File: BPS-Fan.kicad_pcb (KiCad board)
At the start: 2 copper layers, 45 x 34.5 mm, 21 parts, among them J1 LDRBRDConn, J2 FAN1, J3 FAN2, J4 FAN3, J5 FAN4, Q1 BUK9M34-100EX, Q2 BUK9M34-100EX, Q3 BUK9M34-100EX, Q4 BUK9M34-100EX

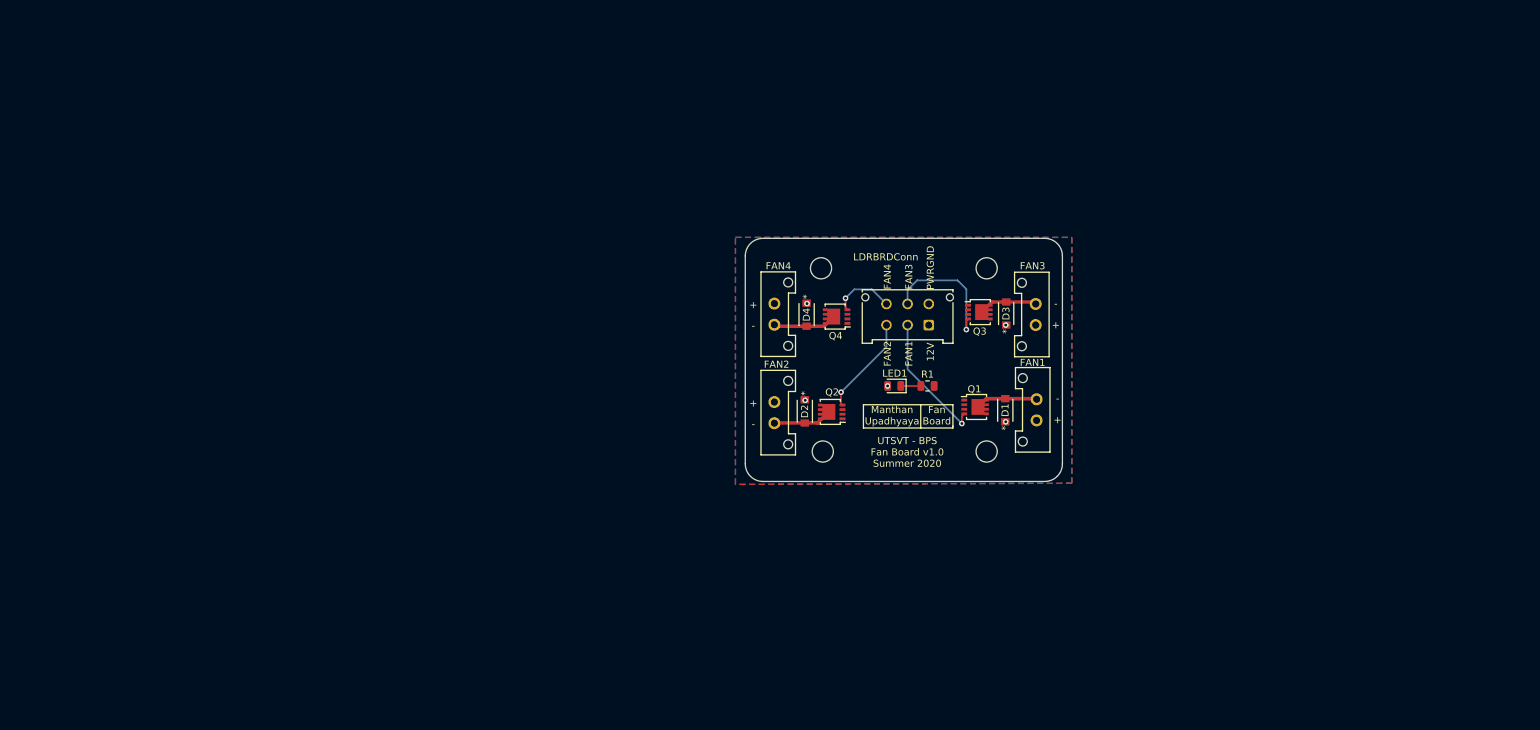
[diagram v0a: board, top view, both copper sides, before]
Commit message: Modified BPS fan pcb schematic to support 12 fans instead of 4.
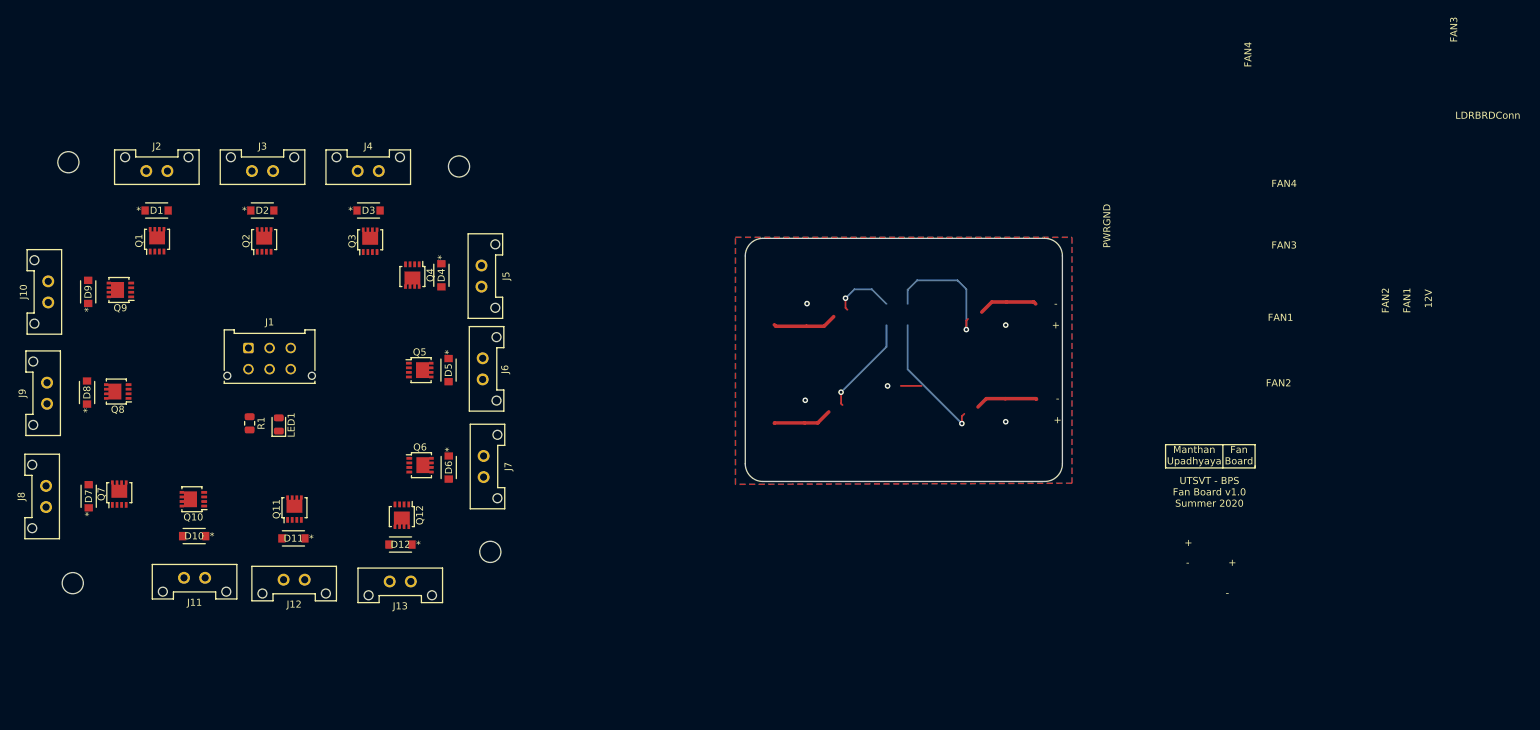
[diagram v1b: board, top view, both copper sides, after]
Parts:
- added D10: V2F22HM, UTSVT_Passive:V2F22HM, F.Cu at (56.8, 97.2)
- added D11: V2F22HM, UTSVT_Passive:V2F22HM, F.Cu at (70.9, 97.6)
- added D12: V2F22HM, UTSVT_Passive:V2F22HM, F.Cu at (86.1, 98.5)
- added D5: V2F22HM, UTSVT_Passive:V2F22HM, F.Cu at (92.9, 73.7)
- added D6: V2F22HM, UTSVT_Passive:V2F22HM, F.Cu at (92.9, 87.5)
- added D7: V2F22HM, UTSVT_Passive:V2F22HM, F.Cu at (41.8, 91.6)
- added D8: V2F22HM, UTSVT_Passive:V2F22HM, F.Cu at (41.6, 76.9)
- added D9: V2F22HM, UTSVT_Passive:V2F22HM, F.Cu at (41.8, 62.6)
- added J10: FAN9, UTSVT_Connectors:Molex_MicroFit3.0_1x2xP3.00mm_PolarizingPeg_Vertical, F.Cu at (36.1, 64.1)
- added J11: FAN10, UTSVT_Connectors:Molex_MicroFit3.0_1x2xP3.00mm_PolarizingPeg_Vertical, F.Cu at (58.4, 103.2)
- added J12: FAN11, UTSVT_Connectors:Molex_MicroFit3.0_1x2xP3.00mm_PolarizingPeg_Vertical, F.Cu at (72.5, 103.4)
- added J13: FAN12, UTSVT_Connectors:Molex_MicroFit3.0_1x2xP3.00mm_PolarizingPeg_Vertical, F.Cu at (87.5, 103.7)
- added J6: FAN5, UTSVT_Connectors:Molex_MicroFit3.0_1x2xP3.00mm_PolarizingPeg_Vertical, F.Cu at (97.7, 72.0)
- added J7: FAN6, UTSVT_Connectors:Molex_MicroFit3.0_1x2xP3.00mm_PolarizingPeg_Vertical, F.Cu at (97.9, 85.9)
- added J8: FAN7, UTSVT_Connectors:Molex_MicroFit3.0_1x2xP3.00mm_PolarizingPeg_Vertical, F.Cu at (35.8, 93.1)
- added J9: FAN8, UTSVT_Connectors:Molex_MicroFit3.0_1x2xP3.00mm_PolarizingPeg_Vertical, F.Cu at (35.9, 78.5)
- added Q10: BUK9M34-100EX, Package_TO_SOT_SMD:LFPAK33, F.Cu at (56.7, 92.0)
- added Q11: BUK9M34-100EX, Package_TO_SOT_SMD:LFPAK33, F.Cu at (71.0, 93.4)
- added Q12: BUK9M34-100EX, Package_TO_SOT_SMD:LFPAK33, F.Cu at (86.3, 94.3)
- added Q5: BUK9M34-100EX, Package_TO_SOT_SMD:LFPAK33, F.Cu at (88.8, 73.7)
- added Q6: BUK9M34-100EX, Package_TO_SOT_SMD:LFPAK33, F.Cu at (88.8, 87.2)
- added Q7: BUK9M34-100EX, Package_TO_SOT_SMD:LFPAK33, F.Cu at (46.2, 91.3)
- added Q8: BUK9M34-100EX, Package_TO_SOT_SMD:LFPAK33, F.Cu at (46.0, 76.7)
- added Q9: BUK9M34-100EX, Package_TO_SOT_SMD:LFPAK33, F.Cu at (46.3, 62.3)
- moved J2 131.2 mm to (50.0, 45.5), turned to 0 degrees
- moved H4 131.0 mm to (39.6, 103.9)
- moved D1 123.7 mm to (51.5, 51.0), turned to 0 degrees
- moved Q1 118.5 mm to (51.5, 55.3), turned to 90 degrees
- moved H1 107.9 mm to (39.0, 44.2)
- moved J4 98.7 mm to (80.0, 45.5), turned to 0 degrees
- moved J1 96.6 mm to (64.5, 70.6), turned to 0 degrees
- moved R1 96.3 mm to (64.7, 81.2), turned to -90 degrees
- moved D3 91.7 mm to (81.5, 51.0), turned to 0 degrees
- moved LED1 87.5 mm to (68.8, 81.4), turned to 90 degrees
- moved Q3 87.0 mm to (81.8, 55.4), turned to 90 degrees
- moved Q2 84.1 mm to (66.7, 55.4), turned to 90 degrees
- moved D2 82.1 mm to (66.5, 51.0), turned to 0 degrees
- moved J3 81.1 mm to (65.0, 45.5), turned to 0 degrees
- moved H3 76.3 mm to (94.4, 44.8)
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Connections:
- D1 pad 1: +12V -> Net-(J2-Pad1)
- D2 pad 1: +12V -> Net-(J2-Pad1)
- D3 pad 1: +12V -> Net-(J2-Pad1)
- D4 pad 1: +12V -> GNDPWR
- J1 pad 2: /FAN1 -> /FAN1CONN
- J1 pad 3: /FAN2 -> /FAN2CONN
- J1 pad 5: /FAN3 -> /FAN3CONN
- J1 pad 6: /FAN4 -> /FAN4CONN
- J2 pad 1: +12V -> Net-(J2-Pad1)
- J3 pad 1: +12V -> Net-(J2-Pad1)
- J4 pad 1: +12V -> Net-(J2-Pad1)
- J5 pad 1: +12V -> GNDPWR
- Q1 pad 4: /FAN1 -> /FAN1CONN
- Q2 pad 4: /FAN2 -> /FAN1CONN
- Q3 pad 4: /FAN3 -> /FAN1CONN
- Q4 pad 4: /FAN4 -> /FAN2CONN
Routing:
- net (no net): track 0.00 -> 46.3 mm, vias 0 -> 2
- net /FAN3: track 18.7 -> 0.00 mm, vias 1 -> 0
- net /FAN1: track 18.7 -> 0.00 mm, vias 1 -> 0
- net Net-(J6-Pad2): track 0.00 -> 14.1 mm, vias 0 -> 1
- net /FAN2: track 14.1 -> 0.00 mm, vias 1 -> 0
- net Net-(J5-Pad2): track 9.08 -> 0.00 mm
- net Net-(J2-Pad1): track 0.00 -> 9.08 mm
- net Net-(D3-Pad2): track 8.37 -> 17.4 mm, vias 0 -> 1
- net /FAN4: track 9.05 -> 0.00 mm, vias 1 -> 0
- net Net-(J2-Pad2): track 8.84 -> 0.00 mm
- net Net-(J3-Pad2): track 8.39 -> 0.00 mm
- net GNDPWR: track 0.00 -> 8.39 mm
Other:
- net class Default removed

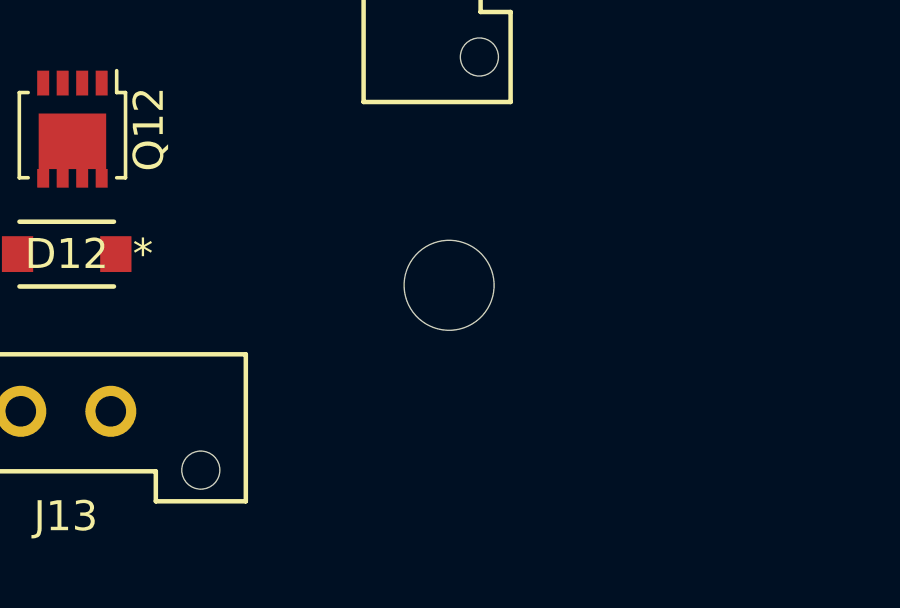
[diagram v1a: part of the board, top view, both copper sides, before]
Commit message: Replaced mosfet, added Hannah's changes, updated bom and data sheets
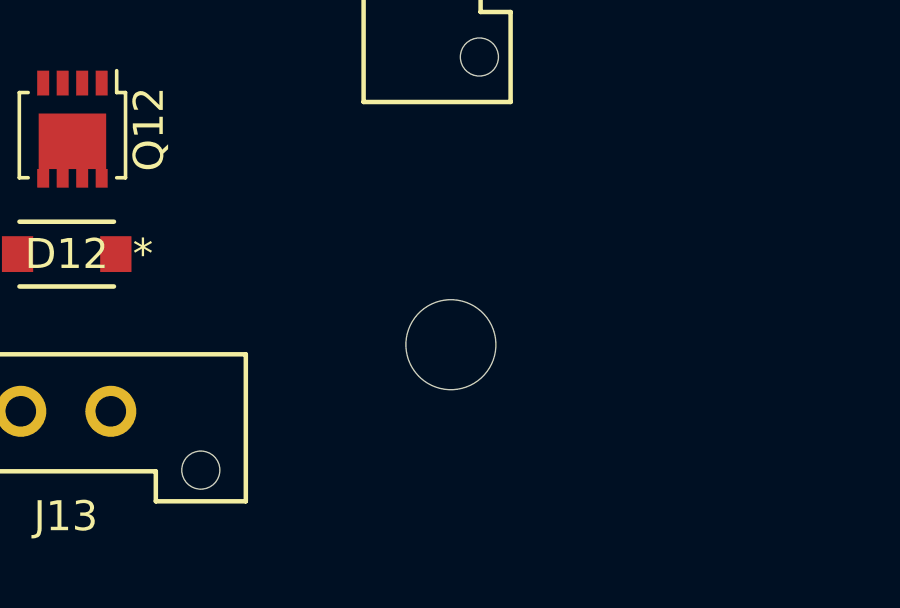
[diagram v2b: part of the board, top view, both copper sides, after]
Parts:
- Q1, Q10, Q11, Q12, Q2, Q3, Q4, Q5, Q6, Q7, Q8, Q9: value BUK9M34-100EX -> BUK9M23-80E
- moved H2 1.98 mm to (98.9, 101.5)
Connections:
- D1 pad 1: Net-(J2-Pad1) -> +12V
- D10 pad 1: GNDPWR -> +12V
- D11 pad 1: GNDPWR -> +12V
- D12 pad 1: GNDPWR -> +12V
- D2 pad 1: Net-(J2-Pad1) -> +12V
- D3 pad 1: Net-(J2-Pad1) -> +12V
- D4 pad 1: GNDPWR -> +12V
- D5 pad 1: GNDPWR -> +12V
- D6 pad 1: GNDPWR -> +12V
- D7 pad 1: GNDPWR -> +12V
- D8 pad 1: GNDPWR -> +12V
- D9 pad 1: GNDPWR -> +12V
- J10 pad 1: GNDPWR -> +12V
- J11 pad 1: GNDPWR -> +12V
- J12 pad 1: GNDPWR -> +12V
- J13 pad 1: GNDPWR -> +12V
- J2 pad 1: Net-(J2-Pad1) -> +12V
- J3 pad 1: Net-(J2-Pad1) -> +12V
- J4 pad 1: Net-(J2-Pad1) -> +12V
- J5 pad 1: GNDPWR -> +12V
- J6 pad 1: GNDPWR -> +12V
- J7 pad 1: GNDPWR -> +12V
- J8 pad 1: GNDPWR -> +12V
- J9 pad 1: GNDPWR -> +12V
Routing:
- net (no net): track 46.3 -> 69.4 mm
- net Net-(D5-Pad2): track 14.1 -> 0.00 mm
- net Net-(J2-Pad1): track 9.08 -> 0.00 mm

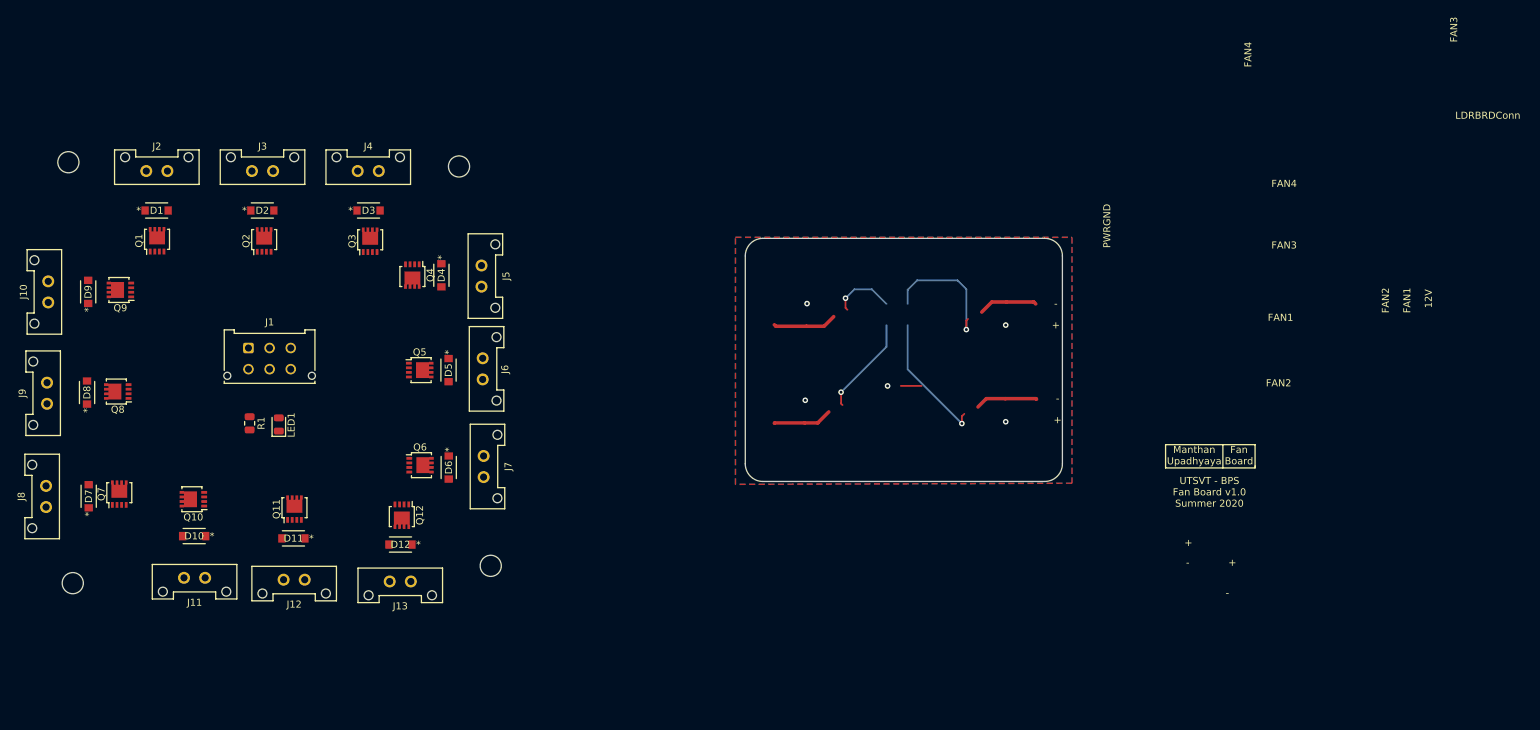
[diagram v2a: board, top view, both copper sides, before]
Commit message: preliminary idea for layout, NOT cleaned up yet!
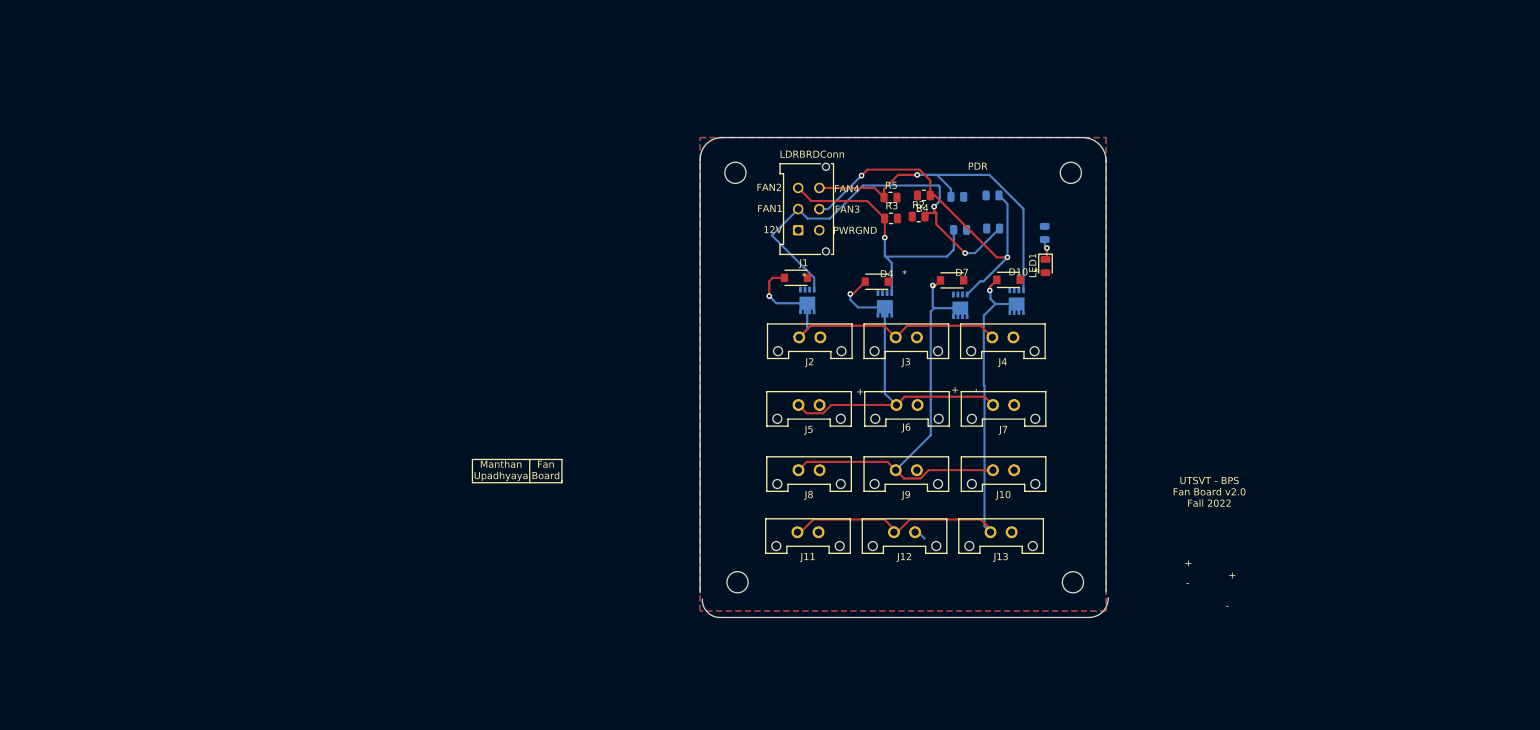
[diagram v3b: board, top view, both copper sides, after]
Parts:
- removed D11, D12, D2, D3, D5, D6, D8, D9: V2F22HM, UTSVT_Passive:V2F22HM
- removed Q11, Q12, Q5, Q6, Q8, Q9: BUK9M23-80E, Package_TO_SOT_SMD:LFPAK33
- removed the Q2 at (66.7, 55.4)
- removed the Q3 at (81.8, 55.4)
- added R2: 100k, Resistor_SMD:R_0805_2012Metric, F.Cu at (159.6, 51.9)
- added R3: 100k, Resistor_SMD:R_0805_2012Metric, F.Cu at (155.7, 52.2)
- added R4: 100k, Resistor_SMD:R_0805_2012Metric, F.Cu at (160.3, 48.9)
- added R5: 100k, Resistor_SMD:R_0805_2012Metric, F.Cu at (155.6, 49.2)
- added R6: 100k, Resistor_SMD:R_0805_2012Metric, B.Cu at (170.2, 53.6)
- added R7: 100k, Resistor_SMD:R_0805_2012Metric, B.Cu at (165.5, 53.8)
- added R8: 100k, Resistor_SMD:R_0805_2012Metric, B.Cu at (170.1, 48.9)
- added R9: 100k, Resistor_SMD:R_0805_2012Metric, B.Cu at (165.1, 49.1)
- Q1: moved to B.Cu
- Q2: renamed from Q4; moved to B.Cu
- Q3: renamed from Q7; moved to B.Cu
- Q4: renamed from Q10; moved to B.Cu
- R1: value 45k -> 10k; moved to B.Cu
- moved J10 139.1 mm to (173.2, 87.9), turned to 180 degrees
- moved D7 126.3 mm to (164.3, 61.0), turned to 180 degrees
- moved J9 123.8 mm to (159.3, 87.9), turned to 180 degrees
- moved Q3 122.3 mm to (165.5, 64.5), turned to -90 degrees
- moved D10 121.1 mm to (172.3, 60.9)
- moved Q4 120.2 mm to (173.5, 63.9), turned to -90 degrees
- moved R1 116.0 mm to (177.5, 54.2), turned to 90 degrees
- moved LED1 111.1 mm to (177.6, 58.9), turned to -90 degrees
- moved J8 109.9 mm to (145.6, 87.9), turned to 180 degrees
- moved J2 98.5 mm to (145.7, 69.0), turned to 180 degrees
- moved J3 97.3 mm to (159.3, 69.0), turned to 180 degrees
- moved J4 96.0 mm to (173.1, 69.0), turned to 180 degrees
- moved H1 94.7 mm to (133.6, 45.7)
- moved H4 94.3 mm to (133.9, 103.8)
- moved Q1 92.7 mm to (143.8, 63.8), turned to -90 degrees
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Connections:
- net /FAN1CONN renamed /FAN1_BPS
- net /FAN2CONN renamed /FAN2_BPS
- net /FAN3CONN renamed /FAN3_BPS
- net /FAN4CONN renamed /FAN4_BPS
- J10 pad 2: Net-(D9-Pad2) -> Net-(D7-Pad2)
- J12 pad 2: Net-(D11-Pad2) -> Net-(D10-Pad2)
- J13 pad 2: Net-(D12-Pad2) -> Net-(D10-Pad2)
- J3 pad 2: Net-(D2-Pad2) -> Net-(D1-Pad2)
- J4 pad 2: Net-(D3-Pad2) -> Net-(D1-Pad2)
- J6 pad 2: Net-(D5-Pad2) -> Net-(D4-Pad2)
- J7 pad 2: Net-(D6-Pad2) -> Net-(D4-Pad2)
- J9 pad 2: Net-(D8-Pad2) -> Net-(D7-Pad2)
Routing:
- net Net-(D10-Pad2): track 0.00 -> 71.0 mm, vias 0 -> 1
- net (no net): track 69.4 -> 0.00 mm, vias 2 -> 0
- net Net-(D7-Pad2): track 0.00 -> 63.6 mm, vias 0 -> 1
- net /FAN1_BPS: track 0.00 -> 58.2 mm, vias 0 -> 2
- net Net-(D4-Pad2): track 0.00 -> 53.5 mm, vias 0 -> 1
- net /FAN3_BPS: track 0.00 -> 52.7 mm, vias 0 -> 2
- net /FAN4_BPS: track 0.00 -> 51.8 mm, vias 0 -> 1
- net Net-(D1-Pad2): track 0.00 -> 46.1 mm, vias 0 -> 1
- net /FAN2_BPS: track 0.00 -> 38.2 mm, vias 0 -> 1
- net Net-(D3-Pad2): track 17.4 -> 0.00 mm, vias 1 -> 0
- net GNDPWR: track 8.39 -> 0.42 mm
- net +12V: track 0.00 -> 4.46 mm, vias 5 -> 0
- net Net-(LED1-Pad1): track 2.95 -> 3.03 mm, vias 0 -> 1
- net Net-(D5-Pad2): vias 1 -> 0
- added copper zone on F.Cu, net +12V
- added copper zone on B.Cu, net GNDPWR
- removed copper zone on B.Cu, net +12V
- removed copper zone on F.Cu, net GNDPWR
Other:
- board size 45 x 34.5 mm -> 57.9 x 68.1 mm
- board text added: "PDR"
- board text added: "UTSVT - BPS Fan Board v2.0 Fall 2022"
- board text removed: "UTSVT - BPS Fan Board v1.0 Summer 2020"
